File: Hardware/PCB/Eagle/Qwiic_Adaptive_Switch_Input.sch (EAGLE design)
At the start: 34 parts, among them J1 QWIIC_RIGHT_ANGLE, J4 QWIIC_RIGHT_ANGLE, SW1 CUI_SJ1-3513, SW2 CUI_SJ1-3513, U1 TCA9534

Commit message: Updated PCB Mount holes
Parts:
- H1, H2: value STAND-OFF -> STAND-OFF-3.3; device SparkFun-Hardware:STAND-OFF -> milador:STAND-OFF-3.3
- JP3, JP4: value STAND-OFF -> STAND-OFF-3.3; device SparkFun:STAND-OFF -> milador:STAND-OFF-3.3
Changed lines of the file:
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@@
 </classes>
 <parts>
-<part name="JP3" library="SparkFun" deviceset="STAND-OFF" device=""/>
-<part name="JP4" library="SparkFun" deviceset="STAND-OFF" device=""/>
+<part name="JP3" library="milador" library_urn="urn:adsk.eagle:library:12595918" deviceset="STAND-OFF-" device="3.3" package3d_urn="urn:adsk.eagle:package:30775189/1"/>
+<part name="JP4" library="milador" library_urn="urn:adsk.eagle:library:12595918" deviceset="STAND-OFF-" device="3.3" package3d_urn="urn:adsk.eagle:package:30775189/1"/>
 <part name="SUPPLY4" library="SparkFun-PowerSymbols" deviceset="3.3V" device=""/>
 <part name="SUPPLY5" library="SparkFun-PowerSymbols" deviceset="3.3V" device=""/>
@@
 <part name="SUPPLY9" library="SparkFun-PowerSymbols" deviceset="3.3V" device=""/>
 <part name="I2C" library="milador_SMD" library_urn="urn:adsk.eagle:library:27847482" deviceset="JUMPERS_JUMPER-SMT_3_2-NC_TRACE" device="_SILK" package3d_urn="urn:adsk.eagle:package:29222217/1"/>
-<part name="H1" library="SparkFun-Hardware" deviceset="STAND-OFF" device=""/>
-<part name="H2" library="SparkFun-Hardware" deviceset="STAND-OFF" device=""/>
+<part name="H1" library="milador" library_urn="urn:adsk.eagle:library:12595918" deviceset="STAND-OFF-" device="3.3" package3d_urn="urn:adsk.eagle:package:30775189/1"/>
+<part name="H2" library="milador" library_urn="urn:adsk.eagle:library:12595918" deviceset="STAND-OFF-" device="3.3" package3d_urn="urn:adsk.eagle:package:30775189/1"/>
 <part name="R3" library="milador_SMD" library_urn="urn:adsk.eagle:library:27847482" deviceset="RESISTOR-" device="0603" package3d_urn="urn:adsk.eagle:package:29222124/2" value="10k"/>
 <part name="SUPPLY12" library="SparkFun-PowerSymbols" deviceset="3.3V" device=""/>

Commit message: Updated footprints to 0805 packages
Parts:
- C1: device milador_SMD:CAP_CERAMIC-0603 -> milador_SMD:CAP_CERAMIC-0805-MP
- R1, R2, R3, R4, R5, R6, R7, R8, R9: device milador_SMD:RESISTOR-0603 -> milador_SMD:RESISTOR-0805-MP
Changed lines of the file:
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@@
 </part>
 <part name="SUPPLY7" library="SparkFun-PowerSymbols" deviceset="3.3V" device=""/>
-<part name="C1" library="milador_SMD" library_urn="urn:adsk.eagle:library:27847482" deviceset="CAP_CERAMIC-" device="0603" package3d_urn="urn:adsk.eagle:package:29222124/2" value="0.1uF"/>
+<part name="C1" library="milador_SMD" library_urn="urn:adsk.eagle:library:27847482" deviceset="CAP_CERAMIC-" device="0805-MP" package3d_urn="urn:adsk.eagle:package:27847629/3" value="0.1uF"/>
 <part name="SUPPLY8" library="SparkFun-PowerSymbols" deviceset="3.3V" device=""/>
 <part name="J4" library="milador_SMD" library_urn="urn:adsk.eagle:library:27847482" deviceset="QWIIC_CONNECTORS" device="JS-1MM" package3d_urn="urn:adsk.eagle:package:29222212/3" value="QWIIC_RIGHT_ANGLE">
 <attribute name="PROD_ID" value="CONN-13694"/>
 </part>
-<part name="R2" library="milador_SMD" library_urn="urn:adsk.eagle:library:27847482" deviceset="RESISTOR-" device="0603" package3d_urn="urn:adsk.eagle:package:29222124/2" value="2.2k"/>
-<part name="R1" library="milador_SMD" library_urn="urn:adsk.eagle:library:27847482" deviceset="RESISTOR-" device="0603" package3d_urn="urn:adsk.eagle:package:29222124/2" value="2.2k"/>
+<part name="R2" library="milador_SMD" library_urn="urn:adsk.eagle:library:27847482" deviceset="RESISTOR-" device="0805-MP" package3d_urn="urn:adsk.eagle:package:27847629/3" value="2.2k"/>
+<part name="R1" library="milador_SMD" library_urn="urn:adsk.eagle:library:27847482" deviceset="RESISTOR-" device="0805-MP" package3d_urn="urn:adsk.eagle:package:27847629/3" value="2.2k"/>
 <part name="SUPPLY1" library="SparkFun-PowerSymbols" deviceset="3.3V" device=""/>
 <part name="U1" library="milador_SMD" library_urn="urn:adsk.eagle:library:27847482" deviceset="TCA9534" device="U" package3d_urn="urn:adsk.eagle:package:29222127/2" value="TCA9534"/>
-<part name="R7" library="milador_SMD" library_urn="urn:adsk.eagle:library:27847482" deviceset="RESISTOR-" device="0603" package3d_urn="urn:adsk.eagle:package:29222124/2" value="2.2k"/>
-<part name="R8" library="milador_SMD" library_urn="urn:adsk.eagle:library:27847482" deviceset="RESISTOR-" device="0603" package3d_urn="urn:adsk.eagle:package:29222124/2" value="2.2k"/>
-<part name="R9" library="milador_SMD" library_urn="urn:adsk.eagle:library:27847482" deviceset="RESISTOR-" device="0603" package3d_urn="urn:adsk.eagle:package:29222124/2" value="2.2k"/>
+<part name="R7" library="milador_SMD" library_urn="urn:adsk.eagle:library:27847482" deviceset="RESISTOR-" device="0805-MP" package3d_urn="urn:adsk.eagle:package:27847629/3" value="2.2k"/>
+<part name="R8" library="milador_SMD" library_urn="urn:adsk.eagle:library:27847482" deviceset="RESISTOR-" device="0805-MP" package3d_urn="urn:adsk.eagle:package:27847629/3" value="2.2k"/>
+<part name="R9" library="milador_SMD" library_urn="urn:adsk.eagle:library:27847482" deviceset="RESISTOR-" device="0805-MP" package3d_urn="urn:adsk.eagle:package:27847629/3" value="2.2k"/>
 <part name="SUPPLY2" library="SparkFun-PowerSymbols" deviceset="3.3V" device=""/>
 <part name="SUPPLY3" library="SparkFun-PowerSymbols" deviceset="3.3V" device=""/>
@@
 <part name="H1" library="milador" library_urn="urn:adsk.eagle:library:12595918" deviceset="STAND-OFF-" device="3.3" package3d_urn="urn:adsk.eagle:package:30775189/1"/>
 <part name="H2" library="milador" library_urn="urn:adsk.eagle:library:12595918" deviceset="STAND-OFF-" device="3.3" package3d_urn="urn:adsk.eagle:package:30775189/1"/>
-<part name="R3" library="milador_SMD" library_urn="urn:adsk.eagle:library:27847482" deviceset="RESISTOR-" device="0603" package3d_urn="urn:adsk.eagle:package:29222124/2" value="10k"/>
+<part name="R3" library="milador_SMD" library_urn="urn:adsk.eagle:library:27847482" deviceset="RESISTOR-" device="0805-MP" package3d_urn="urn:adsk.eagle:package:27847629/3" value="10k"/>
 <part name="SUPPLY12" library="SparkFun-PowerSymbols" deviceset="3.3V" device=""/>
 <part name="INT" library="milador_SMD" library_urn="urn:adsk.eagle:library:27847482" deviceset="JUMPERS-SMT_2_NC_TRACE" device="_SILK" package3d_urn="urn:adsk.eagle:package:29222215/1"/>
@@
 <part name="SUPPLY13" library="SparkFun-PowerSymbols" deviceset="3.3V" device=""/>
 <part name="PWR" library="milador_SMD" library_urn="urn:adsk.eagle:library:27847482" deviceset="JUMPERS-SMT_2_NC_TRACE" device="_SILK" package3d_urn="urn:adsk.eagle:package:29222215/1"/>
-<part name="R4" library="milador_SMD" library_urn="urn:adsk.eagle:library:27847482" deviceset="RESISTOR-" device="0603" package3d_urn="urn:adsk.eagle:package:29222124/2" value="1k"/>
+<part name="R4" library="milador_SMD" library_urn="urn:adsk.eagle:library:27847482" deviceset="RESISTOR-" device="0805-MP" package3d_urn="urn:adsk.eagle:package:27847629/3" value="1k"/>
 <part name="D1" library="milador_SMD" library_urn="urn:adsk.eagle:library:27847482" deviceset="LED" device="" package3d_urn="urn:adsk.eagle:package:29222125/2" value="RED"/>
 <part name="GND8" library="SparkFun-PowerSymbols" deviceset="GND" device=""/>
@@
 <part name="SUPPLY10" library="SparkFun-PowerSymbols" deviceset="3.3V" device=""/>
 <part name="FRAME1" library="frames" library_urn="urn:adsk.eagle:library:229" deviceset="TABL_L" device=""/>
-<part name="R5" library="milador_SMD" library_urn="urn:adsk.eagle:library:27847482" deviceset="RESISTOR-" device="0603" package3d_urn="urn:adsk.eagle:package:29222124/2" value="4.7k"/>
+<part name="R5" library="milador_SMD" library_urn="urn:adsk.eagle:library:27847482" deviceset="RESISTOR-" device="0805-MP" package3d_urn="urn:adsk.eagle:package:27847629/3" value="4.7k"/>
 <part name="SUPPLY11" library="SparkFun-PowerSymbols" deviceset="3.3V" device=""/>
-<part name="R6" library="milador_SMD" library_urn="urn:adsk.eagle:library:27847482" deviceset="RESISTOR-" device="0603" package3d_urn="urn:adsk.eagle:package:29222124/2" value="4.7K"/>
+<part name="R6" library="milador_SMD" library_urn="urn:adsk.eagle:library:27847482" deviceset="RESISTOR-" device="0805-MP" package3d_urn="urn:adsk.eagle:package:27847629/3" value="4.7K"/>
 <part name="SUPPLY15" library="SparkFun-PowerSymbols" deviceset="3.3V" device=""/>
 <part name="ADR2" library="milador_SMD" library_urn="urn:adsk.eagle:library:27847482" deviceset="JUMPERS-SMT_2_NC_TRACE" device="_SILK" package3d_urn="urn:adsk.eagle:package:29222215/1" value="JUMPERS-SMT_2_NC_TRACE_SILK"/>

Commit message: Updated silkscreen
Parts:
- D1: device milador_SMD:LED -> milador_SMD:LED0805_NOOUTLINE
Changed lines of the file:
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@@
 <part name="PWR" library="milador_SMD" library_urn="urn:adsk.eagle:library:27847482" deviceset="JUMPERS-SMT_2_NC_TRACE" device="_SILK" package3d_urn="urn:adsk.eagle:package:29222215/1"/>
 <part name="R4" library="milador_SMD" library_urn="urn:adsk.eagle:library:27847482" deviceset="RESISTOR-" device="0805-MP" package3d_urn="urn:adsk.eagle:package:27847629/3" value="1k"/>
-<part name="D1" library="milador_SMD" library_urn="urn:adsk.eagle:library:27847482" deviceset="LED" device="" package3d_urn="urn:adsk.eagle:package:29222125/2" value="RED"/>
+<part name="D1" library="milador_SMD" library_urn="urn:adsk.eagle:library:27847482" deviceset="LED" device="0805_NOOUTLINE" package3d_urn="urn:adsk.eagle:package:30853605/2" value="RED"/>
 <part name="GND8" library="SparkFun-PowerSymbols" deviceset="GND" device=""/>
 <part name="J2" library="milador" library_urn="urn:adsk.eagle:library:12595918" deviceset="CONNECTORS_CONN_01" device="PTH_NO_SILK_YES_STOP" package3d_urn="urn:adsk.eagle:package:29222250/2"/>

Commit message: Updated design to version 1.2
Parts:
- removed J4: QWIIC_RIGHT_ANGLE, milador_SMD:QWIIC_CONNECTORSJS-1MM
- removed J5: (no value), milador:CONNECTORS_CONN_041X04_NO_SILK
- removed LABEL_14: MILADOR-LOGO-, milador:MILADOR-LOGO-
- removed LABEL_18, LABEL_9: MILADOR-SWITCH-NAME-SW-INPUT, milador:MILADOR-SWITCH-NAME-SW-INPUT
- removed LABEL_2: MILADOR-SWITCH-NAME-SW1, milador:MILADOR-SWITCH-NAME-SW1
- removed LABEL_3: MILADOR-SWITCH-NAME-SW2, milador:MILADOR-SWITCH-NAME-SW2
- added LABEL_!INT_BOTTOM, LABEL_!INT_TOP: MILADOR-LABEL-!INT, milador:MILADOR-LABEL-!INT
- added LABEL_3V_BOTTOM, LABEL_3V_TOP: MILADOR-LABEL-3V, milador:MILADOR-LABEL-3V
- added LABEL_ADR0: MILADOR-LABEL-ADR0, milador:MILADOR-LABEL-ADR0
- added LABEL_ADR1: MILADOR-LABEL-ADR1, milador:MILADOR-LABEL-ADR1
- added LABEL_ADR2: MILADOR-LABEL-ADR2, milador:MILADOR-LABEL-ADR2
- added LABEL_GND_BOTTOM, LABEL_GND_TOP: MILADOR-LABEL-GND, milador:MILADOR-LABEL-GND
- added LABEL_I2C: MILADOR-LABEL-I2C, milador:MILADOR-LABEL-I2C
- added LABEL_I2C_ADDRESS: MILADOR-LABEL-ADDRESS-0X27, milador:MILADOR-LABEL-ADDRESS-0X27
- added LABEL_INPUT_BOTTOM, LABEL_INPUT_TOP: MILADOR-SWITCH-NAME-SW-INPUT, milador:MILADOR-SWITCH-NAME-SW-INPUT
- added LABEL_INT: MILADOR-LABEL-INT, milador:MILADOR-LABEL-INT
- added LABEL_MILADOR_BOTTOM, LABEL_MILADOR_TOP: MILADOR-LOGO-, milador:MILADOR-LOGO-
- added LABEL_P0_BOTTOM: MILADOR-LABEL-P0, milador:MILADOR-LABEL-P0
- added LABEL_P1_BOTTOM: MILADOR-LABEL-P1, milador:MILADOR-LABEL-P1
- added LABEL_P2_BOTTOM, LABEL_P2_TOP: MILADOR-LABEL-P2, milador:MILADOR-LABEL-P2
- added LABEL_P3_BOTTOM, LABEL_P3_TOP: MILADOR-LABEL-P3, milador:MILADOR-LABEL-P3
- added LABEL_PWR: MILADOR-LABEL-PWR, milador:MILADOR-LABEL-PWR
- added LABEL_SW1: MILADOR-SWITCH-NAME-SW1, milador:MILADOR-SWITCH-NAME-SW1
- added LABEL_SW2: MILADOR-SWITCH-NAME-SW2, milador:MILADOR-SWITCH-NAME-SW2
- added LABEL_TITLE_BOTTOM: MILADOR-DEVICE-QWIIC-SWITCH, milador:MILADOR-DEVICE-QWIIC-SWITCH
- added LABEL_TITLE_TOP: MILADOR-DEVICE-QWIIC-SWITCH-SM, milador:MILADOR-DEVICE-QWIIC-SWITCH-SM
- added LABE_SCL_BOTTOM, LABE_SCL_TOP: MILADOR-LABEL-SCL, milador:MILADOR-LABEL-SCL
- added LABE_SDA_BOTTOM, LABE_SDA_TOP: MILADOR-LABEL-SDA, milador:MILADOR-LABEL-SDA
- J2: device milador:CONNECTORS_CONN_01PTH_NO_SILK_YES_STOP -> milador:CONNECTORS_CONN_071X07_NO_SILK
- J3: value (none) -> QWIIC_RIGHT_ANGLE; device milador:CONNECTORS_CONN_041X04_NO_SILK -> milador_SMD:QWIIC_CONNECTORSJS-1MM; PROD_ID (none) -> CONN-13694
- R3: value 10k -> 1k
- R4: value 1k -> 2.2k
- R5: value 4.7k -> 2.2k
- R6: value 4.7K -> 2.2k
- R7, R8: value 2.2k -> 4.7K
- R9: value 2.2k -> 10k
- U1: device milador_SMD:TCA9534U -> milador_SMD:TCA9534DWR
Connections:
- net !INT: now also J2.7, R9.1; no longer J2.1, R3.1
- net 3.3V: now also J2.1, R7.1, R8.1; no longer J4.2, J5.2, R5.2, R6.2
- net ADR0: now also R6.2; no longer R9.2
- net ADR1: now also R5.2; no longer R8.2
- net ADR2: now also R4.2; no longer R7.2
- net GND: now also J2.2, R4.1, R5.1, R6.1; no longer J4.1, J5.1, R7.1, R8.1, R9.1
- net N$1: now also R9.2; no longer R3.2
- net N$2: now also R3.1; no longer R4.1
- net N$3: now also R3.2; no longer R4.2
- net P0: now also R7.2; no longer R5.1
- net P1: now also R8.2; no longer R6.1
- net P2: now also J2.5; no longer J5.3
- net P3: now also J2.6; no longer J5.4
- net SCL: now also J2.3, R2.1; no longer J4.4, R1.1
- net SCL_PU1: now also R1.2; no longer R2.2
- net SDA: now also J2.4, R1.1; no longer J4.3, R2.1
- net SDA_PU1: now also R2.2; no longer R1.2
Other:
- note added: "Output"
- note removed: "Inputs"
- moved on the sheet: ADR0, ADR1, ADR2, C1, J1, R1, R2, R3, R4, R5, R6, R7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

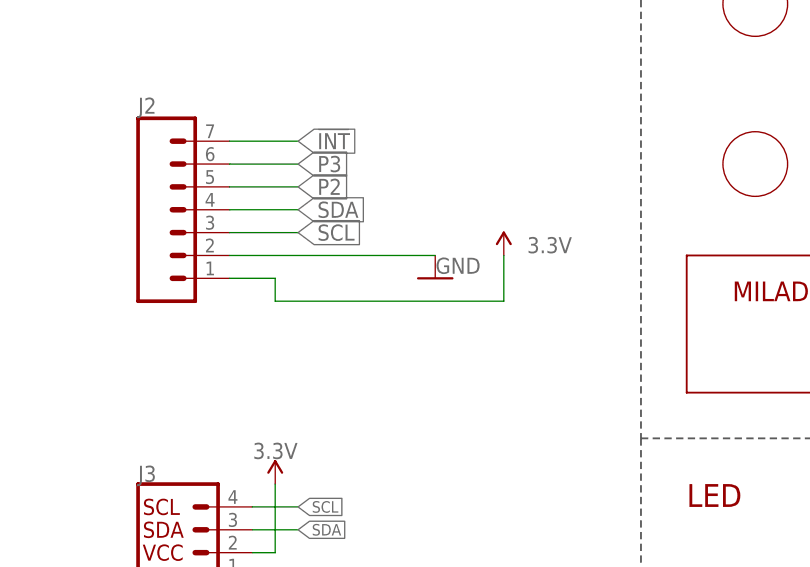
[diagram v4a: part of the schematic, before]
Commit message: Updated header pin order
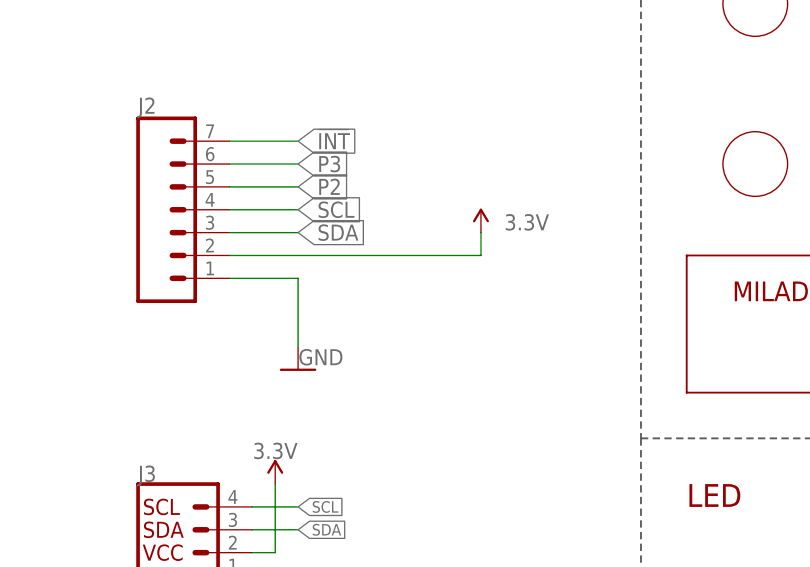
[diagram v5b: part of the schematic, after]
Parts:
- removed JP3: STAND-OFF-3.3, milador:STAND-OFF-3.3
- added H3: STAND-OFF-3.3, milador:STAND-OFF-3.3
- renumbered JP4 to H4
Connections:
- net 3.3V: now also J2.2; no longer J2.1
- net GND: now also J2.1; no longer J2.2
- net SCL: now also J2.4; no longer J2.3
- net SDA: now also J2.3; no longer J2.4
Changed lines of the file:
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@@
 </classes>
 <parts>
-<part name="JP3" library="milador" library_urn="urn:adsk.eagle:library:12595918" deviceset="STAND-OFF-" device="3.3" package3d_urn="urn:adsk.eagle:package:30775189/1"/>
-<part name="JP4" library="milador" library_urn="urn:adsk.eagle:library:12595918" deviceset="STAND-OFF-" device="3.3" package3d_urn="urn:adsk.eagle:package:30775189/1"/>
+<part name="H1" library="milador" library_urn="urn:adsk.eagle:library:12595918" deviceset="STAND-OFF-" device="3.3" package3d_urn="urn:adsk.eagle:package:30775189/1"/>
+<part name="H4" library="milador" library_urn="urn:adsk.eagle:library:12595918" deviceset="STAND-OFF-" device="3.3" package3d_urn="urn:adsk.eagle:package:30775189/1"/>
 <part name="SUPPLY4" library="SparkFun-PowerSymbols" deviceset="3.3V" device=""/>
 <part name="SUPPLY5" library="SparkFun-PowerSymbols" deviceset="3.3V" device=""/>
@@
 <part name="SUPPLY9" library="SparkFun-PowerSymbols" deviceset="3.3V" device=""/>
 <part name="I2C" library="milador_SMD" library_urn="urn:adsk.eagle:library:27847482" deviceset="JUMPERS_JUMPER-SMT_3_2-NC_TRACE" device="_SILK" package3d_urn="urn:adsk.eagle:package:29222217/1"/>
-<part name="H1" library="milador" library_urn="urn:adsk.eagle:library:12595918" deviceset="STAND-OFF-" device="3.3" package3d_urn="urn:adsk.eagle:package:30775189/1"/>
+<part name="H3" library="milador" library_urn="urn:adsk.eagle:library:12595918" deviceset="STAND-OFF-" device="3.3" package3d_urn="urn:adsk.eagle:package:30775189/1"/>
 <part name="H2" library="milador" library_urn="urn:adsk.eagle:library:12595918" deviceset="STAND-OFF-" device="3.3" package3d_urn="urn:adsk.eagle:package:30775189/1"/>
 <part name="R9" library="milador_SMD" library_urn="urn:adsk.eagle:library:27847482" deviceset="RESISTOR-" device="0805-MP" package3d_urn="urn:adsk.eagle:package:27847629/3" value="10k"/>
@@
 </plain>
 <instances>
-<instance part="JP3" gate="G$1" x="233.68" y="226.06" smashed="yes"/>
-<instance part="JP4" gate="G$1" x="233.68" y="213.36" smashed="yes"/>
+<instance part="H1" gate="G$1" x="233.68" y="226.06" smashed="yes"/>
+<instance part="H4" gate="G$1" x="233.68" y="213.36" smashed="yes"/>
 <instance part="SUPPLY4" gate="G$1" x="88.9" y="220.98" smashed="yes" rot="MR0">
 <attribute name="VALUE" x="88.9" y="223.774" size="1.778" layer="96" font="vector" rot="MR0" align="bottom-center"/>
@@
 <attribute name="NAME" x="208.28" y="114.681" size="1.778" layer="95" font="vector" rot="MR0"/>
 </instance>
-<instance part="H1" gate="G$1" x="220.98" y="226.06" smashed="yes"/>
+<instance part="H3" gate="G$1" x="220.98" y="226.06" smashed="yes"/>
 <instance part="H2" gate="G$1" x="220.98" y="213.36" smashed="yes"/>
 <instance part="R9" gate="G$1" x="231.14" y="109.22" smashed="yes" rot="R90">
@@
 <attribute name="NAME" x="73.66" y="185.928" size="1.778" layer="95" font="vector"/>
 </instance>
-<instance part="SUPPLY7" gate="G$1" x="114.3" y="170.18" smashed="yes" rot="MR0">
-<attribute name="VALUE" x="119.38" y="170.434" size="1.778" layer="96" font="vector" rot="MR0" align="bottom-center"/>
-</instance>
-<instance part="GND5" gate="1" x="106.68" y="167.64" smashed="yes">
-<attribute name="VALUE" x="109.22" y="169.926" size="1.778" layer="96" font="vector" align="top-center"/>
+<instance part="SUPPLY7" gate="G$1" x="111.76" y="172.72" smashed="yes" rot="MR0">
+<attribute name="VALUE" x="116.84" y="172.974" size="1.778" layer="96" font="vector" rot="MR0" align="bottom-center"/>
+</instance>
+<instance part="GND5" gate="1" x="91.44" y="157.48" smashed="yes">
+<attribute name="VALUE" x="93.98" y="159.766" size="1.778" layer="96" font="vector" align="top-center"/>
 </instance>
 <instance part="LABEL_3V_TOP" gate="G$1" x="142.24" y="198.12" smashed="yes"/>
@@
 </segment>
 <segment>
-<pinref part="SUPPLY7" gate="G$1" pin="3.3V"/>
-<wire x1="114.3" y1="170.18" x2="114.3" y2="165.1" width="0.1524" layer="91"/>
-<wire x1="114.3" y1="165.1" x2="88.9" y2="165.1" width="0.1524" layer="91"/>
-<wire x1="88.9" y1="165.1" x2="88.9" y2="167.64" width="0.1524" layer="91"/>
-<pinref part="J2" gate="G$1" pin="1"/>
-<wire x1="88.9" y1="167.64" x2="83.82" y2="167.64" width="0.1524" layer="91"/>
-</segment>
-<segment>
 <pinref part="SUPPLY10" gate="G$1" pin="3.3V"/>
 <pinref part="R7" gate="G$1" pin="1"/>
@@
 <pinref part="R8" gate="G$1" pin="1"/>
 <wire x1="182.88" y1="12.7" x2="182.88" y2="10.16" width="0.1524" layer="91"/>
+</segment>
+<segment>
+<pinref part="J2" gate="G$1" pin="2"/>
+<pinref part="SUPPLY7" gate="G$1" pin="3.3V"/>
+<wire x1="83.82" y1="170.18" x2="111.76" y2="170.18" width="0.1524" layer="91"/>
+<wire x1="111.76" y1="170.18" x2="111.76" y2="172.72" width="0.1524" layer="91"/>
 </segment>
 </net>
@@
 </segment>
 <segment>
-<pinref part="J2" gate="G$1" pin="2"/>
+<pinref part="J2" gate="G$1" pin="1"/>
 <pinref part="GND5" gate="1" pin="GND"/>
-<wire x1="83.82" y1="170.18" x2="106.68" y2="170.18" width="0.1524" layer="91"/>
+<wire x1="83.82" y1="167.64" x2="91.44" y2="167.64" width="0.1524" layer="91"/>
+<wire x1="91.44" y1="167.64" x2="91.44" y2="160.02" width="0.1524" layer="91"/>
 </segment>
 </net>
@@
 </segment>
 <segment>
-<pinref part="J2" gate="G$1" pin="4"/>
-<wire x1="83.82" y1="175.26" x2="91.44" y2="175.26" width="0.1524" layer="91"/>
-<label x="91.44" y="175.26" size="1.778" layer="95" xref="yes"/>
+<pinref part="J2" gate="G$1" pin="3"/>
+<wire x1="83.82" y1="172.72" x2="91.44" y2="172.72" width="0.1524" layer="91"/>
+<label x="91.44" y="172.72" size="1.778" layer="95" xref="yes"/>
 </segment>
 </net>
@@
 </segment>
 <segment>
-<pinref part="J2" gate="G$1" pin="3"/>
-<wire x1="83.82" y1="172.72" x2="91.44" y2="172.72" width="0.1524" layer="91"/>
-<label x="91.44" y="172.72" size="1.778" layer="95" xref="yes"/>
-</segment>
-</net>
+<pinref part="J2" gate="G$1" pin="4"/>
+<wire x1="83.82" y1="175.26" x2="91.44" y2="175.26" width="0.1524" layer="91"/>
+<label x="91.44" y="175.26" size="1.778" layer="95" xref="yes"/>
+</segment>
+</net>
